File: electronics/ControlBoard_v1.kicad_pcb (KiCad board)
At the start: 2 copper layers, 64 x 85 mm, 28 parts, among them J1 Motor1, J2 Motor2, J3 Motor3, J4 Encoder, J5 I2C, J7 Power, U1 ROB-14450, U2 ROB-14450, U3 ROB-14450, U4 DCDC_Converter

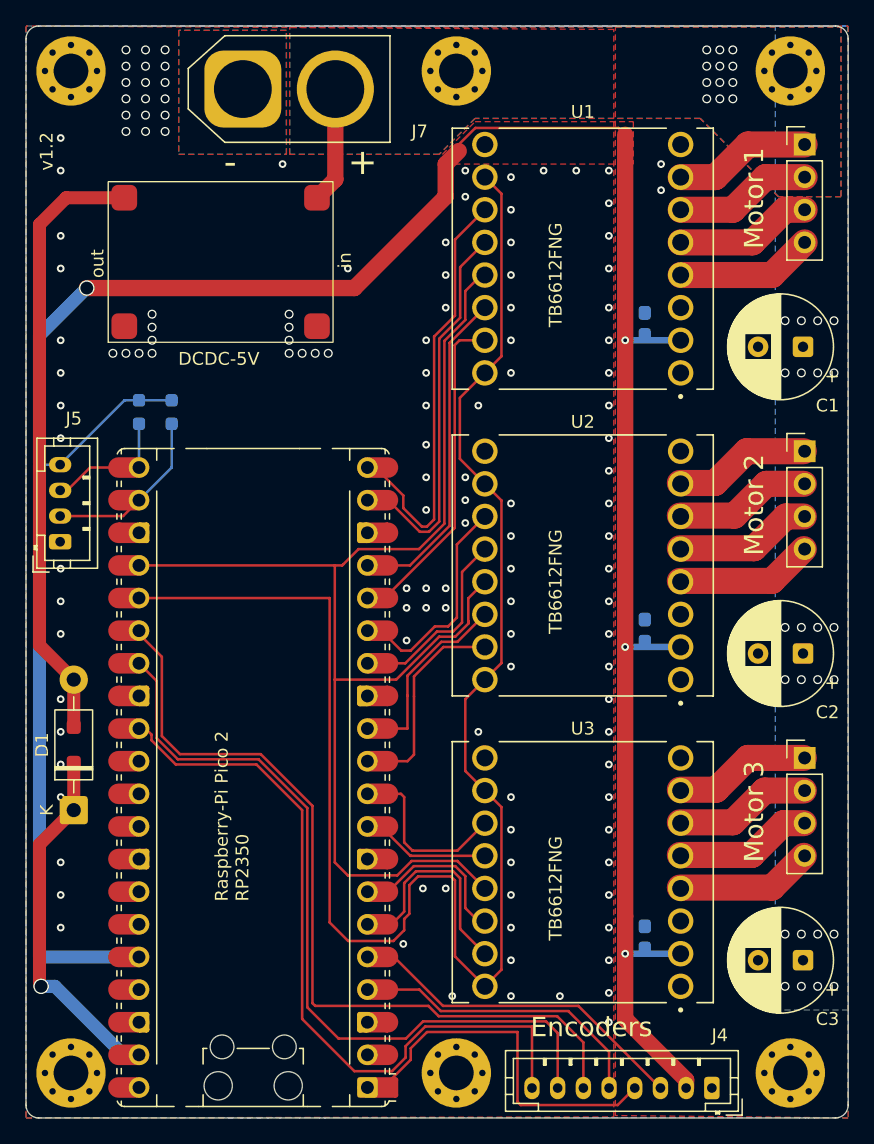
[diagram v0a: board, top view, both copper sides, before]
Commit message: fixed critical problem in PCB layout, where a misplaced via shorted 5V rail to GND
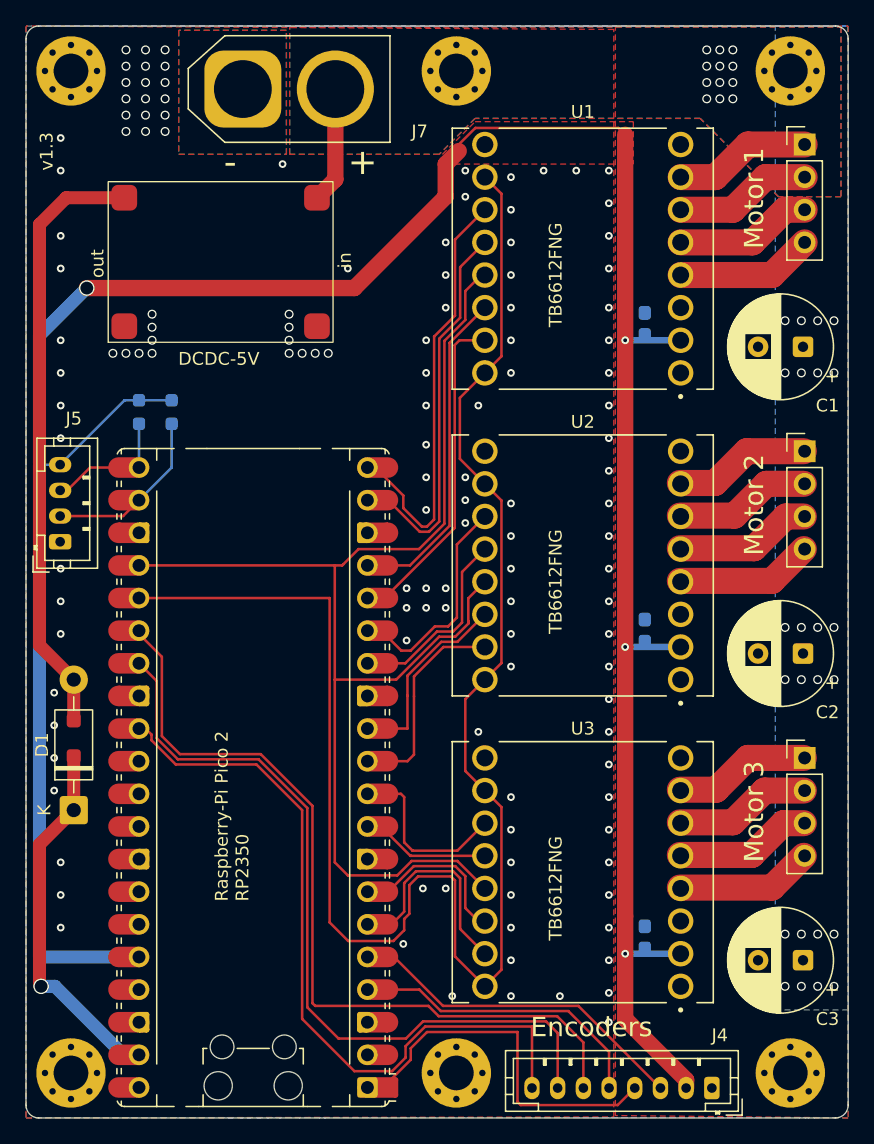
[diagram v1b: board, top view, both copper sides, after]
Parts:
- moved D2 0.51 mm to (158.5, 94.6)
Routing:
- net Net-(D1-A): track 47.7 -> 47.2 mm
- net GND: vias 131 -> 129
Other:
- board text added: "v1.3"
- board text removed: "v1.2"
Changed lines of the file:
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@@
 	(footprint "Diode_SMD:D_SOD-123F"
 		(layer "F.Cu")
-		(at 158.496 95.076 90)
+		(at 158.496 94.568 90)
 		(descr "D_SOD-123F")
 		(tags "D_SOD-123F")
@@
 		)
 		(fp_text user "K"
-			(at 0 -2.1 90)
+			(at 0 -2.286 90)
 			(layer "F.SilkS")
 			(effects
@@
 		)
 	)
-	(gr_text "v1.2"
+	(gr_text "v1.3"
 		(at 156.972 50.372 90)
 		(layer "F.SilkS")
@@
 	)
 	(via
-		(at 157.48 96.6)
+		(at 156.972 96.092)
 		(size 0.6)
 		(drill 0.3)
@@
 	)
 	(via
-		(at 157.48 94.06)
+		(at 156.972 93.552)
 		(size 0.6)
 		(drill 0.3)
@@
 	)
 	(via
-		(at 157.48 99.14)
+		(at 156.972 98.632)
 		(size 0.6)
 		(drill 0.3)
@@
 	)
 	(via
-		(at 157.48 91.52)
+		(at 156.972 91.012)
 		(size 0.6)
 		(drill 0.3)
@@
 	)
 	(via
-		(at 204.216 49.864)
-		(size 0.6)
-		(drill 0.3)
-		(layers "F.Cu" "B.Cu")
-		(free yes)
-		(net 3)
-	)
-	(via
 		(at 164.592 62.564)
 		(size 0.7)
@@
 	)
 	(via
-		(at 204.216 51.896)
-		(size 0.6)
-		(drill 0.3)
-		(layers "F.Cu" "B.Cu")
-		(free yes)
-		(net 3)
-	)
-	(via
 		(at 164.084 46.054)
 		(size 0.7)
@@
 	)
 	(segment
-		(start 158.496 89.996)
-		(end 158.496 93.676)
+		(start 157.908 52.484)
+		(end 162.43 52.484)
 		(width 1.016)
 		(layer "F.Cu")
@@
 	)
 	(segment
-		(start 157.908 52.484)
-		(end 162.43 52.484)
+		(start 155.829 54.563)
+		(end 157.908 52.484)
 		(width 1.016)
 		(layer "F.Cu")
@@
 	)
 	(segment
-		(start 155.829 54.563)
-		(end 157.908 52.484)
+		(start 158.496 89.996)
+		(end 158.496 93.168)
 		(width 1.016)
 		(layer "F.Cu")
